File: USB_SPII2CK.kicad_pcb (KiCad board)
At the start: 2 copper layers, 50 x 31 mm, 46 parts, among them J1 Conn_02x05_Odd_Even, J2 Conn_01x02, J3 Conn_01x02, J4 USB_B_Micro, J5 Conn_01x02, J6 Conn_02x08_Odd_Even, U1 LP2985-3.3, U2 FT2232HL, U3 AT93C46DN-SH-T, Y1 12.00 MHz

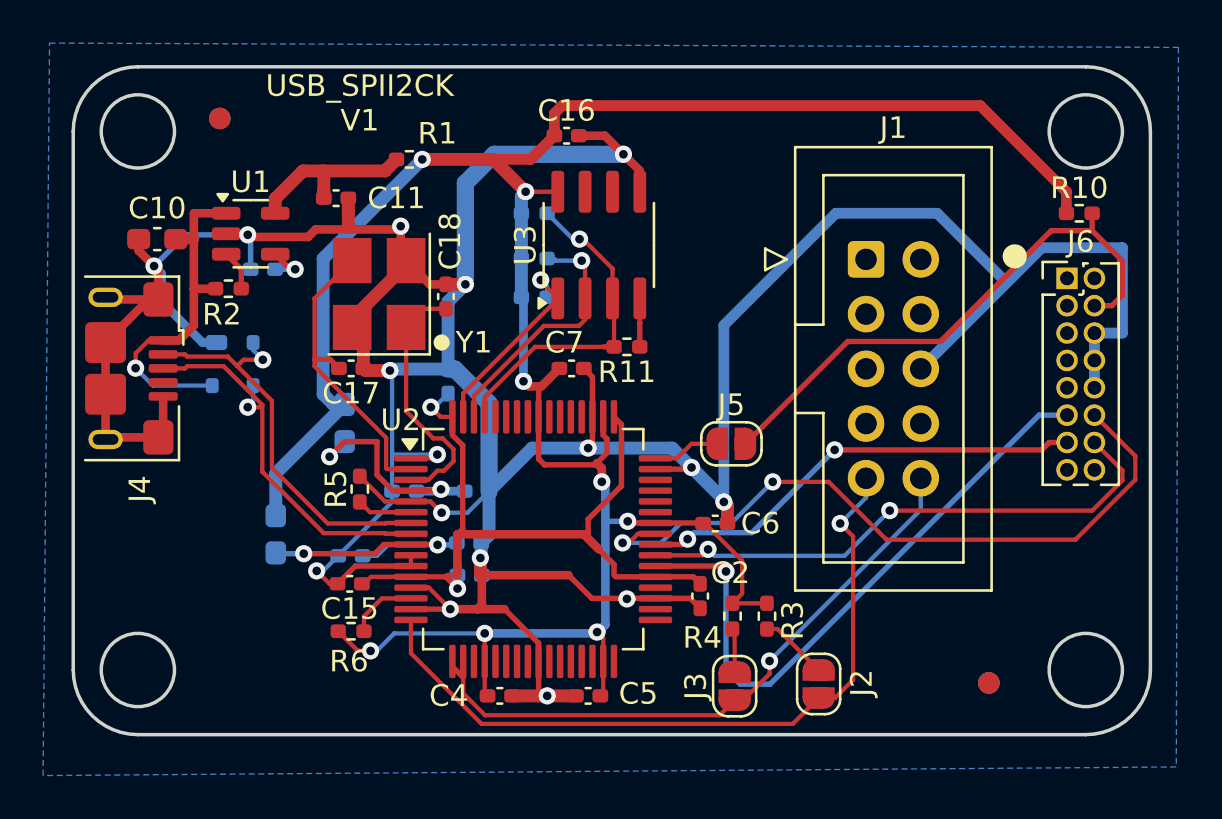
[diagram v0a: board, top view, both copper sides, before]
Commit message: Update to V1.1 (move R10 out from under connector)
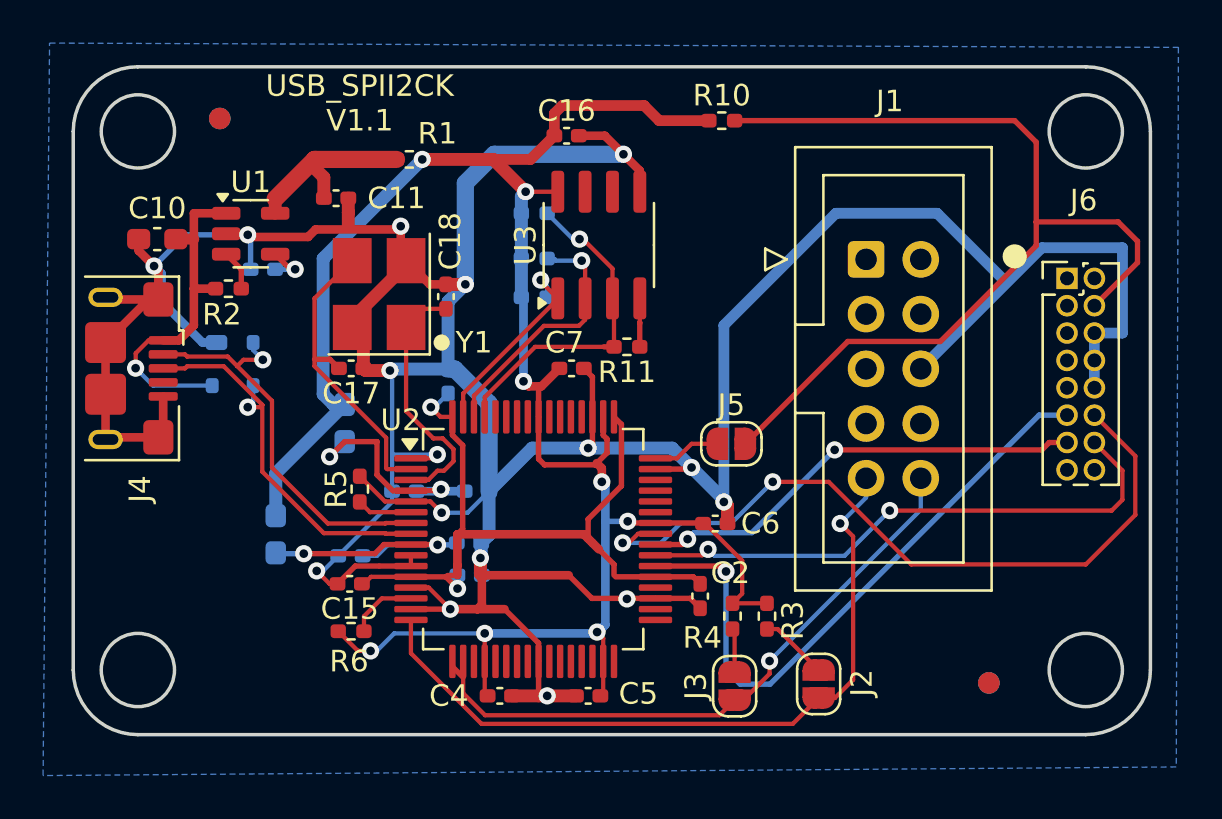
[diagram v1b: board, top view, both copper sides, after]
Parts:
- moved R10 17.1 mm to (152.8, 86.2)
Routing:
- net /~{RESET}: track 26.1 -> 45.4 mm
- net +3.3V: track 116.8 -> 97.8 mm
- net /SPI_SSN: track 32.7 -> 34.6 mm
- net Net-(U1-VOUT): track 8.66 -> 9.24 mm
- net /SPI_MOSI: track 25.7 -> 26.2 mm
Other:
- board text added: "USB_SPII2CK V1.1"
- board text removed: "USB_SPII2CK V1"
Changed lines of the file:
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@@
 		(tags "Through hole vertical IDC box header THT 2x05 2.54mm double row")
 		(property "Reference" "J1"
-			(at 1.27 -6.1 0)
+			(at 1.1 -7.34 0)
 			(layer "F.SilkS")
 			(effects
@@
 	(footprint "Resistor_SMD:R_0402_1005Metric_Pad0.72x0.64mm_HandSolder"
 		(layer "F.Cu")
-		(at 169.3975 90.5)
+		(at 152.8025 86.2)
 		(descr "Resistor SMD 0402 (1005 Metric), square (rectangular) end terminal, IPC_7351 nominal with elongated pad for handsoldering. (Body size source: IPC-SM-782 page 72, https://www.pcb-3d.com/wordpress/wp-content/uploads/ipc-sm-782a_amendment_1_and_2.pdf), generated with kicad-footprint-generator")
 		(tags "resistor handsolder")
@@
 		(tags "Through hole pin header THT 2x08 1.27mm double row")
 		(property "Reference" "J6"
-			(at 0.635 -1.695 0)
+			(at 0.77 -3.62 0)
 			(layer "F.SilkS")
 			(effects
@@
 			)
 		)
+		(property "LCSC" "C17282974"
+			(at 0 0 0)
+			(unlocked yes)
+			(layer "F.Fab")
+			(hide yes)
+			(effects
+				(font
+					(size 1 1)
+					(thickness 0.15)
+				)
+			)
+		)
 		(property ki_fp_filters "Connector*:*_2x??_*")
 		(sheetname "Root")
@@
 		(layer "Edge.Cuts")
 	)
-	(gr_text "USB_SPII2CK\nV1"
+	(gr_text "USB_SPII2CK\nV1.1"
 		(at 136 84 0)
 		(layer "F.SilkS")
@@
 	)
 	(segment
-		(start 143.932 88)
-		(end 145.032 86.9)
-		(width 0.5)
-		(layer "F.Cu")
-		(net 3)
-	)
-	(segment
 		(start 148.512 104.875)
 		(end 148.437 104.799)
@@
 	)
 	(segment
-		(start 145.4 85.5)
-		(end 164.8 85.5)
-		(width 0.5)
-		(layer "F.Cu")
-		(net 3)
-	)
-	(segment
 		(start 153.75 108.154)
 		(end 153.75 106.623)
@@
 	)
 	(segment
-		(start 142.2 88)
-		(end 143.932 88)
-		(width 0.5)
-		(layer "F.Cu")
-		(net 3)
-	)
-	(segment
-		(start 164.8 85.5)
-		(end 168.8 89.5)
+		(start 149.2 85.5)
+		(end 145.4 85.5)
 		(width 0.5)
 		(layer "F.Cu")
@@
 	)
 	(segment
-		(start 168.8 89.5)
-		(end 168.8 90.5)
-		(width 0.5)
-		(layer "F.Cu")
-		(net 3)
-	)
-	(segment
 		(start 147.477 100.978)
 		(end 147.3 100.801)
@@
 	)
 	(segment
+		(start 152.205 86.2)
+		(end 149.9 86.2)
+		(width 0.5)
+		(layer "F.Cu")
+		(net 3)
+	)
+	(segment
 		(start 144.3 101.9)
 		(end 144.577 102.177)
@@
 	)
 	(segment
+		(start 143.932 88)
+		(end 142.2 88)
+		(width 0.5)
+		(layer "F.Cu")
+		(net 3)
+	)
+	(segment
 		(start 147.3 111.3)
 		(end 147.3 110.225)
@@
 	)
 	(segment
+		(start 145.4 85.5)
+		(end 145.032 85.8675)
+		(width 0.5)
+		(layer "F.Cu")
+		(net 3)
+	)
+	(segment
 		(start 135.913 110.813)
 		(end 135 109.9)
@@
 	)
 	(segment
+		(start 145.032 85.8675)
+		(end 145.032 86.9)
+		(width 0.5)
+		(layer "F.Cu")
+		(net 3)
+	)
+	(segment
 		(start 145.032 86.9)
-		(end 145.032 85.8675)
+		(end 143.932 88)
+		(width 0.5)
+		(layer "F.Cu")
+		(net 3)
+	)
+	(segment
+		(start 149.9 86.2)
+		(end 149.2 85.5)
 		(width 0.5)
 		(layer "F.Cu")
@@
 	)
 	(segment
-		(start 145.032 85.8675)
-		(end 145.4 85.5)
-		(width 0.5)
-		(layer "F.Cu")
-		(net 3)
-	)
-	(segment
 		(start 154.9 108.605)
 		(end 153.302 108.605)
@@
 	)
 	(segment
-		(start 133.365 88.535)
+		(start 132.075 90.5)
 		(end 132.075 89.825)
 		(width 0.6)
@@
 	)
 	(segment
-		(start 133.365 88.535)
-		(end 137.17 88.535)
-		(width 0.6)
-		(layer "F.Cu")
-		(net 6)
-	)
-	(segment
-		(start 134.332 88.567)
-		(end 134.3 88.535)
-		(width 0.6)
-		(layer "F.Cu")
-		(net 6)
-	)
-	(segment
-		(start 137.705 88)
-		(end 137.17 88.535)
+		(start 134.332 89.8)
+		(end 134.332 88.832)
 		(width 0.6)
 		(layer "F.Cu")
@@
 	)
 	(segment
-		(start 134.332 89.8)
-		(end 134.332 89.4837)
+		(start 134.332 88.832)
+		(end 133.7 88.2)
 		(width 0.6)
 		(layer "F.Cu")
@@
 	(segment
 		(start 134.332 89.4837)
-		(end 134.332 88.567)
-		(width 0.6)
+		(end 134.332 89.8)
+		(width 0.5)
 		(layer "F.Cu")
 		(net 6)
@@
 	(segment
 		(start 132.075 89.825)
-		(end 132.075 90.5)
-		(width 0.6)
+		(end 133.9 88)
+		(width 0.8)
 		(layer "F.Cu")
 		(net 6)
 	)
 	(segment
-		(start 134.332 89.4837)
-		(end 134.332 89.8)
-		(width 0.5)
+		(start 133.9 88)
+		(end 137.705 88)
+		(width 0.8)
 		(layer "F.Cu")
 		(net 6)
@@
 	)
 	(segment
-		(start 171.4 92.71)
-		(end 169.995 91.305)
+		(start 166.4 86.2)
+		(end 167.4 87.2)
 		(width 0.25)
 		(layer "F.Cu")
@@
 	)
 	(segment
-		(start 168.095 91.305)
-		(end 169.995 91.305)
+		(start 153.4 86.2)
+		(end 166.4 86.2)
 		(width 0.25)
 		(layer "F.Cu")
@@
 	)
 	(segment
-		(start 153.9 101.2)
-		(end 158.65 96.45)
+		(start 172.1 91.8)
+		(end 171.2 90.9)
+		(width 0.25)
+		(layer "F.Cu")
+		(net 25)
+	)
+	(segment
+		(start 158.65 96.45)
+		(end 162.95 96.45)
 		(width 0.25)
 		(layer "F.Cu")
@@
 	)
 	(segment
-		(start 170.91 94.79)
-		(end 171.4 94.3)
+		(start 170.1 94.79)
+		(end 172.1 92.79)
 		(width 0.25)
 		(layer "F.Cu")
@@
 	)
 	(segment
-		(start 171.4 94.3)
-		(end 171.4 92.71)
+		(start 153.9 101.2)
+		(end 158.65 96.45)
 		(width 0.25)
 		(layer "F.Cu")
@@
 	)
 	(segment
-		(start 169.995 91.305)
-		(end 169.995 90.5)
+		(start 167.4 87.2)
+		(end 167.4 90.9)
 		(width 0.25)
 		(layer "F.Cu")
@@
 	)
 	(segment
-		(start 158.65 96.45)
-		(end 162.95 96.45)
+		(start 172.1 92.79)
+		(end 172.1 91.8)
+		(width 0.25)
+		(layer "F.Cu")
+		(net 25)
+	)
+	(segment
+		(start 171.2 90.9)
+		(end 167.4 90.9)
 		(width 0.25)
 		(layer "F.Cu")
@@
 	(segment
 		(start 162.95 96.45)
-		(end 168.095 91.305)
+		(end 167.4 92)
 		(width 0.25)
 		(layer "F.Cu")
@@
 	)
 	(segment
-		(start 170.1 94.79)
-		(end 170.91 94.79)
+		(start 167.4 92)
+		(end 167.4 90.9)
 		(width 0.25)
 		(layer "F.Cu")
@@
 	)
 	(segment
-		(start 171.4 102.9)
-		(end 170 104.3)
+		(start 171.4 102.44)
+		(end 171.4 103.8)
 		(width 0.2)
 		(layer "F.Cu")
@@
 	)
 	(segment
-		(start 171.4 102.44)
-		(end 171.4 102.9)
+		(start 151.891 106.375)
+		(end 152.166 106.1)
 		(width 0.2)
 		(layer "F.Cu")
@@
 	)
 	(segment
-		(start 151.891 106.375)
-		(end 152.166 106.1)
+		(start 171.4 103.8)
+		(end 170.9 104.3)
 		(width 0.2)
 		(layer "F.Cu")
@@
 	)
 	(segment
-		(start 170 104.3)
+		(start 170.9 104.3)
 		(end 160.6 104.3)
 		(width 0.2)
@@
 	)
 	(segment
-		(start 148.2 105.8)
-		(end 148.493 105.8)
+		(start 172 101.77)
+		(end 172 104.5)
 		(width 0.2)
 		(layer "F.Cu")
@@
 	)
 	(segment
-		(start 157.767 102.967)
-		(end 155.167 102.967)
+		(start 161.6 106.8)
+		(end 157.767 102.967)
 		(width 0.2)
 		(layer "F.Cu")
@@
 	)
 	(segment
-		(start 172 102.866)
-		(end 169.216 105.65)
+		(start 148.2 105.8)
+		(end 148.493 105.8)
 		(width 0.2)
 		(layer "F.Cu")
@@
 	)
 	(segment
-		(start 160.45 105.65)
-		(end 157.767 102.967)
+		(start 157.767 102.967)
+		(end 155.167 102.967)
 		(width 0.2)
 		(layer "F.Cu")
@@
 	)
 	(segment
-		(start 172 101.77)
-		(end 172 102.866)
+		(start 172 104.5)
+		(end 169.7 106.8)
 		(width 0.2)
 		(layer "F.Cu")
@@
 	)
 	(segment
-		(start 169.216 105.65)
-		(end 160.45 105.65)
+		(start 169.7 106.8)
+		(end 161.6 106.8)
 		(width 0.2)
 		(layer "F.Cu")
